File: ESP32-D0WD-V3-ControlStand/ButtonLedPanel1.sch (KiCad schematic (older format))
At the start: 31 parts

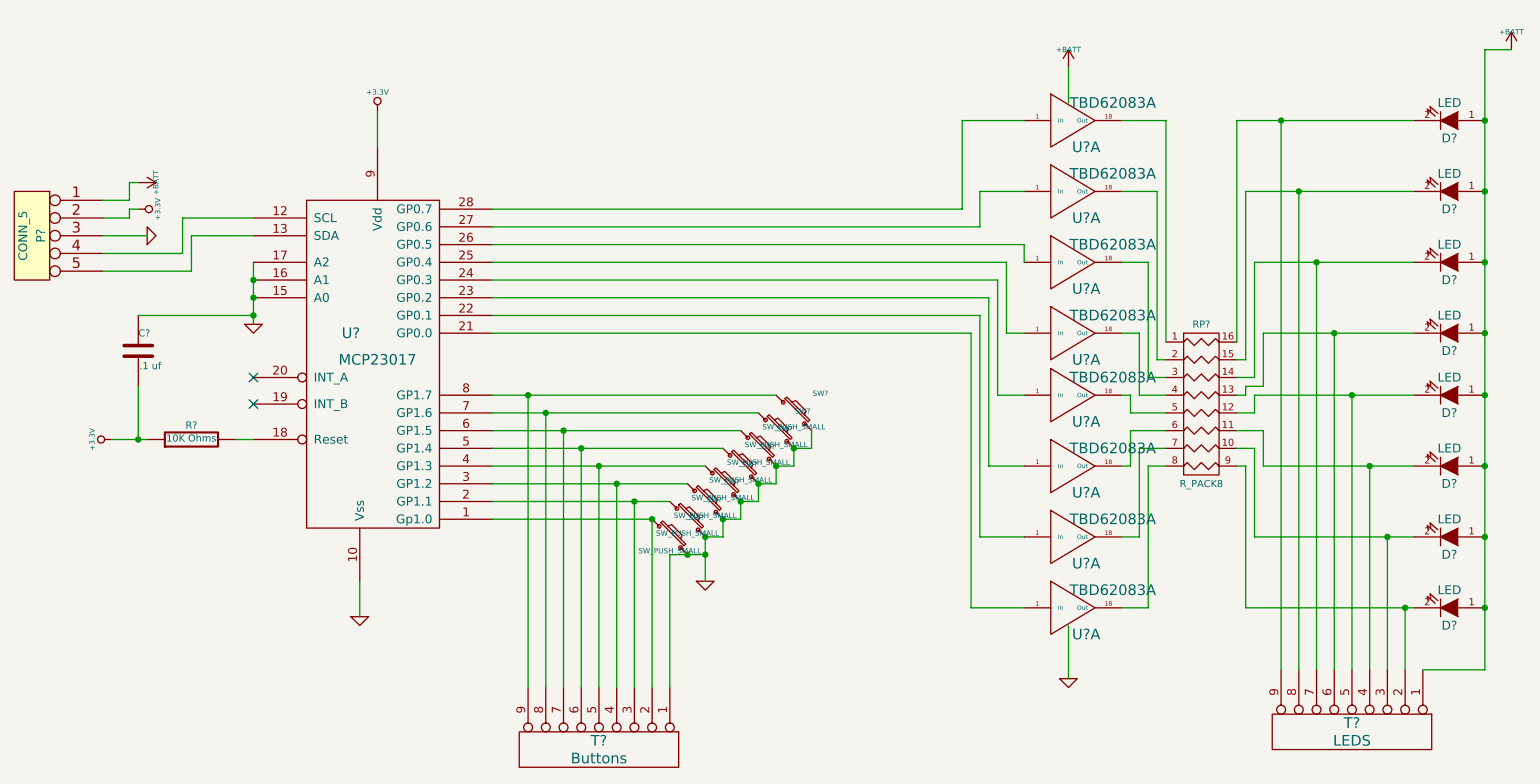
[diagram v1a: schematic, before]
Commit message: Completed parts spec for ESP32-D0WD-V3-ControlStand.
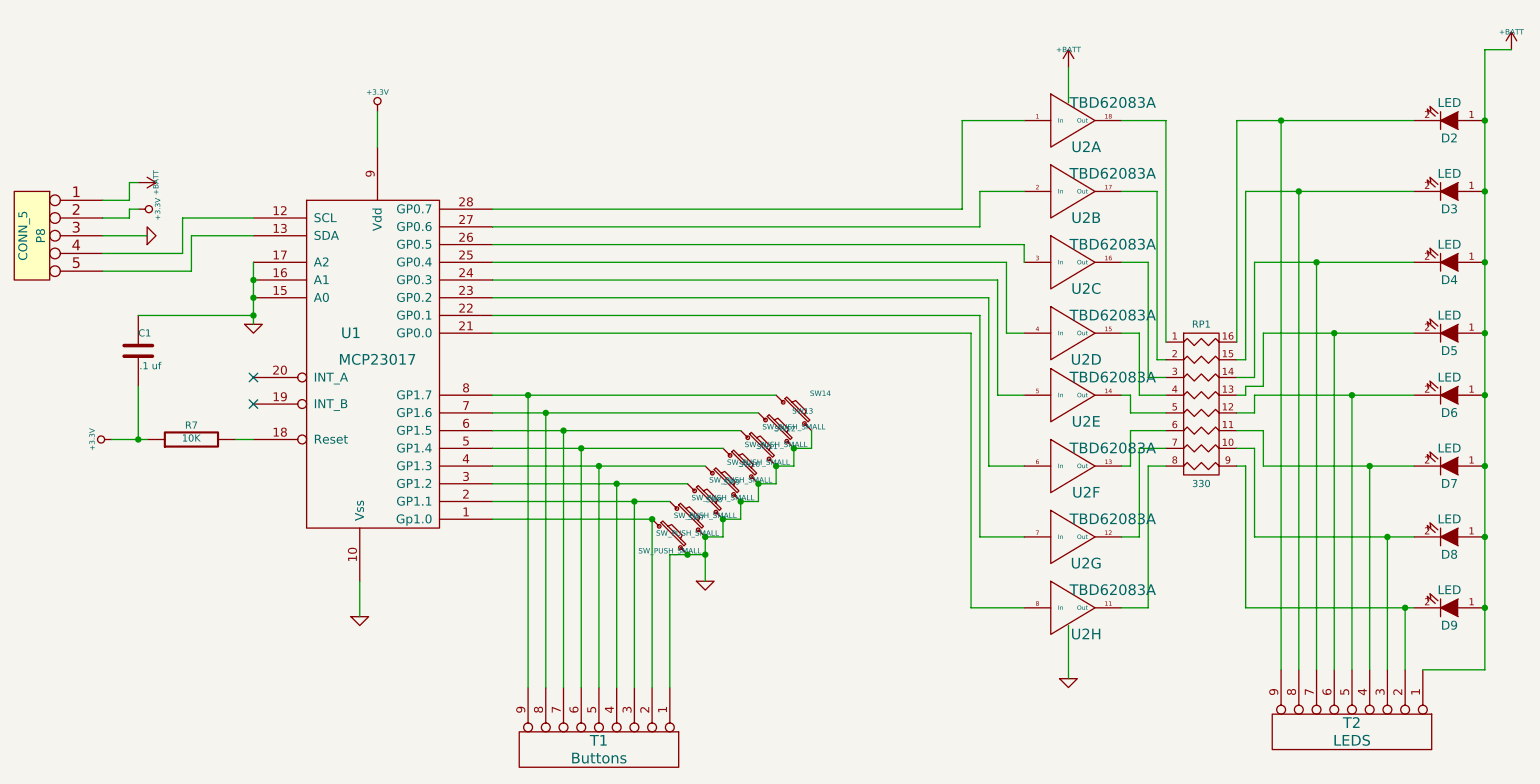
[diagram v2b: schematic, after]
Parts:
- C1: renamed from C?; footprint ~ -> Capacitors_SMD:C_0603; Mouser Part Number (none) -> 710-885012206095
- D2, D3, D4, D5, D6, D7, D8, D9: renamed from D?; footprint ~ -> LEDs:LED_D5.0mm
- P8: renamed from P?; footprint ~ -> Pin_Headers:Pin_Header_Angled_1x05_Pitch2.54mm; Mouser Part Number (none) -> 649-1012937990501BLF
- R7: renamed from R?; value 10K Ohms -> 10K; footprint ~ -> Resistors_SMD:R_0402; Mouser Part Number (none) -> 603-RC0402JR-0710KL
- RP1: renamed from RP?; value R_PACK8 -> 330; footprint ~ -> 48xxP:4816P; Mouser Part Number (none) -> 652-4816P-T1LF-330
- SW10, SW11, SW12, SW13, SW14: renamed from SW?; footprint ~ -> Buttons_Switches_THT:SW_PUSH_6mm; Mouser Part Number (none) -> 179-TS026660BK160LCR
- SW7, SW8, SW9: renamed from SW?; footprint ~ -> Buttons_Switches_THT:SW_PUSH_6m; Mouser Part Number (none) -> 179-TS026660BK160LCR
- T1: renamed from T?; footprint ~ -> Terminal_Blocks:TerminalBlock_Pheonix_MPT-2.54mm_9pol; Mouser Part Number (none) -> 651-1725724
- T2: renamed from T?; footprint ~ -> Connectors_Terminal_Blocks:TerminalBlock_Pheonix_MPT-2.54mm_9pol; Mouser Part Number (none) -> 651-1725724
- U1: renamed from U?; footprint ~ -> Housings_SOIC:SOIC-28W_7.5x17.9mm_Pitch1.27mm; Mouser Part Number (none) -> 579-MCP23017-E/SO
- U2: renamed from U?; footprint ~ -> Housings_SOIC:SOIC-18W_7.5x11.6mm_Pitch1.27mm; Mouser Part Number (none) -> 757-TBD62083AFG
- gave numbers to parts that had none: 1
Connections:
- net at U1.21 (GP0.0): now also U2.8 (In); no longer U2.1 (In)
- net at U1.22 (GP0.1): now also U2.7 (In); no longer U2.1 (In)
- net at U1.23 (GP0.2): now also U2.6 (In); no longer U2.1 (In)
- net at U1.24 (GP0.3): now also U2.5 (In); no longer U2.1 (In)
- net at U1.25 (GP0.4): now also U2.4 (In); no longer U2.1 (In)
- net at U1.26 (GP0.5): now also U2.3 (In); no longer U2.1 (In)
- net at U1.27 (GP0.6): now also U2.2 (In); no longer U2.1 (In)
- net at RP1.2 (P2): now also U2.17 (Out); no longer U2.18 (Out)
- net at RP1.3 (P3): now also U2.16 (Out); no longer U2.18 (Out)
- net at RP1.4 (P4): now also U2.15 (Out); no longer U2.18 (Out)
- net at RP1.5 (P5): now also U2.14 (Out); no longer U2.18 (Out)
- net at RP1.6 (P6): now also U2.13 (Out); no longer U2.18 (Out)
- net at RP1.7 (P7): now also U2.12 (Out); no longer U2.18 (Out)
- net at RP1.8 (P8): now also U2.11 (Out); no longer U2.18 (Out)

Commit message: Working on the PCB Layout.
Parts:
- added MK10, MK11, MK12, MK9: Mounting_Hole, Mounting_Holes:MountingHole_2.5mm, symbol Mounting_Hole
- SW7, SW8, SW9: footprint Buttons_Switches_THT:SW_PUSH_6m -> Buttons_Switches_THT:SW_PUSH_6mm
- U2: footprint ~ -> Housings_SOIC:SOIC-18W_7.5x11.6mm_Pitch1.27mm
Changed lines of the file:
@@
 LIBS:mcp73871
 LIBS:lm2574n-5
+LIBS:mechanical
+LIBS:graphic_symbols
 LIBS:ESP32-D0WD-V3-ControlStand-cache
 EELAYER 25 0
@@
 F 0 "U2" H 8100 1300 60  0000 C CNN
 F 1 "TBD62083A" H 8250 1550 60  0000 C CNN
-F 2 "~" H 8000 1450 60  0000 C CNN
+F 2 "Housings_SOIC:SOIC-18W_7.5x11.6mm_Pitch1.27mm" H 8000 1450 60  0001 C CNN
 F 3 "~" H 8000 1450 60  0000 C CNN
 	2    8000 1450
@@
 F 0 "U2" H 8100 1700 60  0000 C CNN
 F 1 "TBD62083A" H 8250 1950 60  0000 C CNN
-F 2 "~" H 8000 1850 60  0000 C CNN
+F 2 "Housings_SOIC:SOIC-18W_7.5x11.6mm_Pitch1.27mm" H 8000 1850 60  0001 C CNN
 F 3 "~" H 8000 1850 60  0000 C CNN
 	3    8000 1850
@@
 F 0 "U2" H 8100 2100 60  0000 C CNN
 F 1 "TBD62083A" H 8250 2350 60  0000 C CNN
-F 2 "~" H 8000 2250 60  0000 C CNN
+F 2 "Housings_SOIC:SOIC-18W_7.5x11.6mm_Pitch1.27mm" H 8000 2250 60  0001 C CNN
 F 3 "~" H 8000 2250 60  0000 C CNN
 	4    8000 2250
@@
 F 0 "U2" H 8100 2450 60  0000 C CNN
 F 1 "TBD62083A" H 8250 2700 60  0000 C CNN
-F 2 "~" H 8000 2600 60  0000 C CNN
+F 2 "Housings_SOIC:SOIC-18W_7.5x11.6mm_Pitch1.27mm" H 8000 2600 60  0001 C CNN
 F 3 "~" H 8000 2600 60  0000 C CNN
 	5    8000 2600
@@
 F 0 "U2" H 8100 2850 60  0000 C CNN
 F 1 "TBD62083A" H 8250 3100 60  0000 C CNN
-F 2 "~" H 8000 3000 60  0000 C CNN
+F 2 "Housings_SOIC:SOIC-18W_7.5x11.6mm_Pitch1.27mm" H 8000 3000 60  0001 C CNN
 F 3 "~" H 8000 3000 60  0000 C CNN
 	6    8000 3000
@@
 F 0 "U2" H 8100 3250 60  0000 C CNN
 F 1 "TBD62083A" H 8250 3500 60  0000 C CNN
-F 2 "~" H 8000 3400 60  0000 C CNN
+F 2 "Housings_SOIC:SOIC-18W_7.5x11.6mm_Pitch1.27mm" H 8000 3400 60  0001 C CNN
 F 3 "~" H 8000 3400 60  0000 C CNN
 	7    8000 3400
@@
 F 0 "U2" H 8100 3650 60  0000 C CNN
 F 1 "TBD62083A" H 8250 3900 60  0000 C CNN
-F 2 "~" H 8000 3800 60  0000 C CNN
+F 2 "Housings_SOIC:SOIC-18W_7.5x11.6mm_Pitch1.27mm" H 8000 3800 60  0001 C CNN
 F 3 "~" H 8000 3800 60  0000 C CNN
 	8    8000 3800
@@
 F 0 "SW7" H 5900 3510 30  0000 C CNN
 F 1 "SW_PUSH_SMALL" H 5750 3321 30  0000 C CNN
-F 2 "Buttons_Switches_THT:SW_PUSH_6m" H 5750 3400 60  0001 C CNN
+F 2 "Buttons_Switches_THT:SW_PUSH_6mm" H 5750 3400 60  0001 C CNN
 F 3 "~" H 5750 3400 60  0000 C CNN
 F 4 "179-TS026660BK160LCR" H 5750 3400 60  0001 C CNN "Mouser Part Number"
@@
 F 0 "SW9" H 6100 3310 30  0000 C CNN
 F 1 "SW_PUSH_SMALL" H 5950 3121 30  0000 C CNN
-F 2 "Buttons_Switches_THT:SW_PUSH_6m" H 5950 3200 60  0001 C CNN
+F 2 "Buttons_Switches_THT:SW_PUSH_6mm" H 5950 3200 60  0001 C CNN
 F 3 "~" H 5950 3200 60  0000 C CNN
 F 4 "179-TS026660BK160LCR" H 5950 3200 60  0001 C CNN "Mouser Part Number"
@@
 F 0 "SW8" H 6000 3410 30  0000 C CNN
 F 1 "SW_PUSH_SMALL" H 5850 3221 30  0000 C CNN
-F 2 "Buttons_Switches_THT:SW_PUSH_6m" H 5850 3300 60  0001 C CNN
+F 2 "Buttons_Switches_THT:SW_PUSH_6mm" H 5850 3300 60  0001 C CNN
 F 3 "~" H 5850 3300 60  0000 C CNN
 F 4 "179-TS026660BK160LCR" H 5850 3300 60  0001 C CNN "Mouser Part Number"
@@
 	5950 3400 5950 3650
 $Comp
-L GND-RESCUE-ESP32ControlStand #PWR25
+L GND-RESCUE-ESP32ControlStand #PWR018
 U 1 1 62DF1D4E
 P 5950 3650
-F 0 "#PWR25" H 5950 3650 30  0001 C CNN
+F 0 "#PWR018" H 5950 3650 30  0001 C CNN
 F 1 "GND" H 5950 3580 30  0001 C CNN
 F 2 "" H 5950 3650 60  0000 C CNN
@@
 $EndComp
 $Comp
-L +BATT #PWR26
+L +BATT #PWR019
 U 1 1 62DF1D58
 P 8000 750
-F 0 "#PWR26" H 8000 700 20  0001 C CNN
+F 0 "#PWR019" H 8000 700 20  0001 C CNN
 F 1 "+BATT" H 8000 850 30  0000 C CNN
 F 2 "" H 8000 750 60  0000 C CNN
@@
 $EndComp
 $Comp
-L GND-RESCUE-ESP32ControlStand #PWR27
+L GND-RESCUE-ESP32ControlStand #PWR020
 U 1 1 62DF1D59
 P 8000 4200
-F 0 "#PWR27" H 8000 4200 30  0001 C CNN
+F 0 "#PWR020" H 8000 4200 30  0001 C CNN
 F 1 "GND" H 8000 4130 30  0001 C CNN
 F 2 "" H 8000 4200 60  0000 C CNN
@@
 $EndComp
 $Comp
-L +BATT #PWR28
+L +BATT #PWR021
 U 1 1 62DF1D5A
 P 10500 650
-F 0 "#PWR28" H 10500 600 20  0001 C CNN
+F 0 "#PWR021" H 10500 600 20  0001 C CNN
 F 1 "+BATT" H 10500 750 30  0000 C CNN
 F 2 "" H 10500 650 60  0000 C CNN
@@
 Connection ~ 10350 1050
 $Comp
-L GND-RESCUE-ESP32ControlStand #PWR23
+L GND-RESCUE-ESP32ControlStand #PWR022
 U 1 1 62DF1D5B
 P 4000 3850
-F 0 "#PWR23" H 4000 3850 30  0001 C CNN
+F 0 "#PWR022" H 4000 3850 30  0001 C CNN
 F 1 "GND" H 4000 3780 30  0001 C CNN
 F 2 "" H 4000 3850 60  0000 C CNN
@@
 	4000 3650 4000 3850
 $Comp
-L +3.3V-RESCUE-ESP32ControlStand #PWR24
+L +3.3V-RESCUE-ESP32ControlStand #PWR023
 U 1 1 62DF1D5C
 P 4100 1000
-F 0 "#PWR24" H 4100 960 30  0001 C CNN
+F 0 "#PWR023" H 4100 960 30  0001 C CNN
 F 1 "+3.3V" H 4100 1110 30  0000 C CNN
 F 2 "" H 4100 1000 60  0000 C CNN
@@
 Connection ~ 3400 1950
 $Comp
-L GND-RESCUE-ESP32ControlStand #PWR22
+L GND-RESCUE-ESP32ControlStand #PWR024
 U 1 1 62DF1D5D
 P 3400 2200
-F 0 "#PWR22" H 3400 2200 30  0001 C CNN
+F 0 "#PWR024" H 3400 2200 30  0001 C CNN
 F 1 "GND" H 3400 2130 30  0001 C CNN
 F 2 "" H 3400 2200 60  0000 C CNN
@@
 $EndComp
 $Comp
-L +3.3V-RESCUE-ESP32ControlStand #PWR18
+L +3.3V-RESCUE-ESP32ControlStand #PWR025
 U 1 1 62DF1D5F
 P 2600 2850
-F 0 "#PWR18" H 2600 2810 30  0001 C CNN
+F 0 "#PWR025" H 2600 2810 30  0001 C CNN
 F 1 "+3.3V" H 2600 2960 30  0000 C CNN
 F 2 "" H 2600 2850 60  0000 C CNN
@@
 $EndComp
 $Comp
-L +BATT #PWR19
+L +BATT #PWR026
 U 1 1 62DF1D61
 P 2750 1400
-F 0 "#PWR19" H 2750 1350 20  0001 C CNN
+F 0 "#PWR026" H 2750 1350 20  0001 C CNN
 F 1 "+BATT" H 2750 1500 30  0000 C CNN
 F 2 "" H 2750 1400 60  0000 C CNN
@@
 $EndComp
 $Comp
-L +3.3V-RESCUE-ESP32ControlStand #PWR20
+L +3.3V-RESCUE-ESP32ControlStand #PWR027
 U 1 1 62DF1D62
 P 2750 1550
-F 0 "#PWR20" H 2750 1510 30  0001 C CNN
+F 0 "#PWR027" H 2750 1510 30  0001 C CNN
 F 1 "+3.3V" H 2750 1660 30  0000 C CNN
 F 2 "" H 2750 1550 60  0000 C CNN
@@
 $EndComp
 $Comp
-L GND-RESCUE-ESP32ControlStand #PWR21
+L GND-RESCUE-ESP32ControlStand #PWR028
 U 1 1 62DF1D63
 P 2800 1700
-F 0 "#PWR21" H 2800 1700 30  0001 C CNN
+F 0 "#PWR028" H 2800 1700 30  0001 C CNN
 F 1 "GND" H 2800 1630 30  0001 C CNN
 F 2 "" H 2800 1700 60  0000 C CNN
@@
 	2750 2150 3400 2150
 Connection ~ 3400 2150
+$Comp
+L Mounting_Hole MK9
+U 1 1 62E6E9BE
+P 8500 700
+F 0 "MK9" H 8500 900 50  0000 C CNN
+F 1 "Mounting_Hole" H 8500 825 50  0000 C CNN
+F 2 "Mounting_Holes:MountingHole_2.5mm" H 8500 700 50  0001 C CNN
+F 3 "" H 8500 700 50  0001 C CNN
+	1    8500 700
+	1    0    0    -1
+$EndComp
+$Comp
+L Mounting_Hole MK10
+U 1 1 62E6EA13
+P 8750 700
+F 0 "MK10" H 8750 900 50  0000 C CNN
+F 1 "Mounting_Hole" H 8750 825 50  0000 C CNN
+F 2 "Mounting_Holes:MountingHole_2.5mm" H 8750 700 50  0001 C CNN
+F 3 "" H 8750 700 50  0001 C CNN
+	1    8750 700
+	1    0    0    -1
+$EndComp
+$Comp
+L Mounting_Hole MK11
+U 1 1 62E6EA6A
+P 9050 700
+F 0 "MK11" H 9050 900 50  0000 C CNN
+F 1 "Mounting_Hole" H 9050 825 50  0000 C CNN
+F 2 "Mounting_Holes:MountingHole_2.5mm" H 9050 700 50  0001 C CNN
+F 3 "" H 9050 700 50  0001 C CNN
+	1    9050 700
+	1    0    0    -1
+$EndComp
+$Comp
+L Mounting_Hole MK12
+U 1 1 62E6EAD3
+P 9300 700
+F 0 "MK12" H 9300 900 50  0000 C CNN
+F 1 "Mounting_Hole" H 9300 825 50  0000 C CNN
+F 2 "Mounting_Holes:MountingHole_2.5mm" H 9300 700 50  0001 C CNN
+F 3 "" H 9300 700 50  0001 C CNN
+	1    9300 700
+	1    0    0    -1
+$EndComp
 $EndSCHEMATC

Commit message: Completed V0.0 PCB.
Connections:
- net +3.3V renamed +3V3
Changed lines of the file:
@@
 	5950 3400 5950 3650
 $Comp
-L GND-RESCUE-ESP32ControlStand #PWR018
+L GND #PWR020
 U 1 1 62DF1D4E
 P 5950 3650
-F 0 "#PWR018" H 5950 3650 30  0001 C CNN
+F 0 "#PWR020" H 5950 3650 30  0001 C CNN
 F 1 "GND" H 5950 3580 30  0001 C CNN
 F 2 "" H 5950 3650 60  0000 C CNN
@@
 $EndComp
 $Comp
-L +BATT #PWR019
+L +BATT #PWR021
 U 1 1 62DF1D58
 P 8000 750
-F 0 "#PWR019" H 8000 700 20  0001 C CNN
+F 0 "#PWR021" H 8000 700 20  0001 C CNN
 F 1 "+BATT" H 8000 850 30  0000 C CNN
 F 2 "" H 8000 750 60  0000 C CNN
@@
 $EndComp
 $Comp
-L GND-RESCUE-ESP32ControlStand #PWR020
+L GND #PWR022
 U 1 1 62DF1D59
 P 8000 4200
-F 0 "#PWR020" H 8000 4200 30  0001 C CNN
+F 0 "#PWR022" H 8000 4200 30  0001 C CNN
 F 1 "GND" H 8000 4130 30  0001 C CNN
 F 2 "" H 8000 4200 60  0000 C CNN
@@
 $EndComp
 $Comp
-L +BATT #PWR021
+L +BATT #PWR023
 U 1 1 62DF1D5A
 P 10500 650
-F 0 "#PWR021" H 10500 600 20  0001 C CNN
+F 0 "#PWR023" H 10500 600 20  0001 C CNN
 F 1 "+BATT" H 10500 750 30  0000 C CNN
 F 2 "" H 10500 650 60  0000 C CNN
@@
 Connection ~ 10350 1050
 $Comp
-L GND-RESCUE-ESP32ControlStand #PWR022
+L GND #PWR024
 U 1 1 62DF1D5B
 P 4000 3850
-F 0 "#PWR022" H 4000 3850 30  0001 C CNN
+F 0 "#PWR024" H 4000 3850 30  0001 C CNN
 F 1 "GND" H 4000 3780 30  0001 C CNN
 F 2 "" H 4000 3850 60  0000 C CNN
@@
 	4000 3650 4000 3850
 $Comp
-L +3.3V-RESCUE-ESP32ControlStand #PWR023
+L +3.3V #PWR025
 U 1 1 62DF1D5C
 P 4100 1000
-F 0 "#PWR023" H 4100 960 30  0001 C CNN
+F 0 "#PWR025" H 4100 960 30  0001 C CNN
 F 1 "+3.3V" H 4100 1110 30  0000 C CNN
 F 2 "" H 4100 1000 60  0000 C CNN
@@
 Connection ~ 3400 1950
 $Comp
-L GND-RESCUE-ESP32ControlStand #PWR024
+L GND #PWR026
 U 1 1 62DF1D5D
 P 3400 2200
-F 0 "#PWR024" H 3400 2200 30  0001 C CNN
+F 0 "#PWR026" H 3400 2200 30  0001 C CNN
 F 1 "GND" H 3400 2130 30  0001 C CNN
 F 2 "" H 3400 2200 60  0000 C CNN
@@
 $EndComp
 $Comp
-L +3.3V-RESCUE-ESP32ControlStand #PWR025
+L +3.3V #PWR027
 U 1 1 62DF1D5F
 P 2600 2850
-F 0 "#PWR025" H 2600 2810 30  0001 C CNN
+F 0 "#PWR027" H 2600 2810 30  0001 C CNN
 F 1 "+3.3V" H 2600 2960 30  0000 C CNN
 F 2 "" H 2600 2850 60  0000 C CNN
@@
 $EndComp
 $Comp
-L +BATT #PWR026
+L +BATT #PWR028
 U 1 1 62DF1D61
 P 2750 1400
-F 0 "#PWR026" H 2750 1350 20  0001 C CNN
+F 0 "#PWR028" H 2750 1350 20  0001 C CNN
 F 1 "+BATT" H 2750 1500 30  0000 C CNN
 F 2 "" H 2750 1400 60  0000 C CNN
@@
 $EndComp
 $Comp
-L +3.3V-RESCUE-ESP32ControlStand #PWR027
+L +3.3V #PWR029
 U 1 1 62DF1D62
 P 2750 1550
-F 0 "#PWR027" H 2750 1510 30  0001 C CNN
+F 0 "#PWR029" H 2750 1510 30  0001 C CNN
 F 1 "+3.3V" H 2750 1660 30  0000 C CNN
 F 2 "" H 2750 1550 60  0000 C CNN
@@
 $EndComp
 $Comp
-L GND-RESCUE-ESP32ControlStand #PWR028
+L GND #PWR030
 U 1 1 62DF1D63
 P 2800 1700
-F 0 "#PWR028" H 2800 1700 30  0001 C CNN
+F 0 "#PWR030" H 2800 1700 30  0001 C CNN
 F 1 "GND" H 2800 1630 30  0001 C CNN
 F 2 "" H 2800 1700 60  0000 C CNN
